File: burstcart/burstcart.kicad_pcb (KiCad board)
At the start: 2 copper layers, 56 x 91 mm, 17 parts, among them J1 IEC, J2 IEC, J3 BURST, J4 PORTA, U1 27C512, U2 CD74HCT4520E, U3 6526 CIA, U4 20V8, U5 ATtiny85-20P

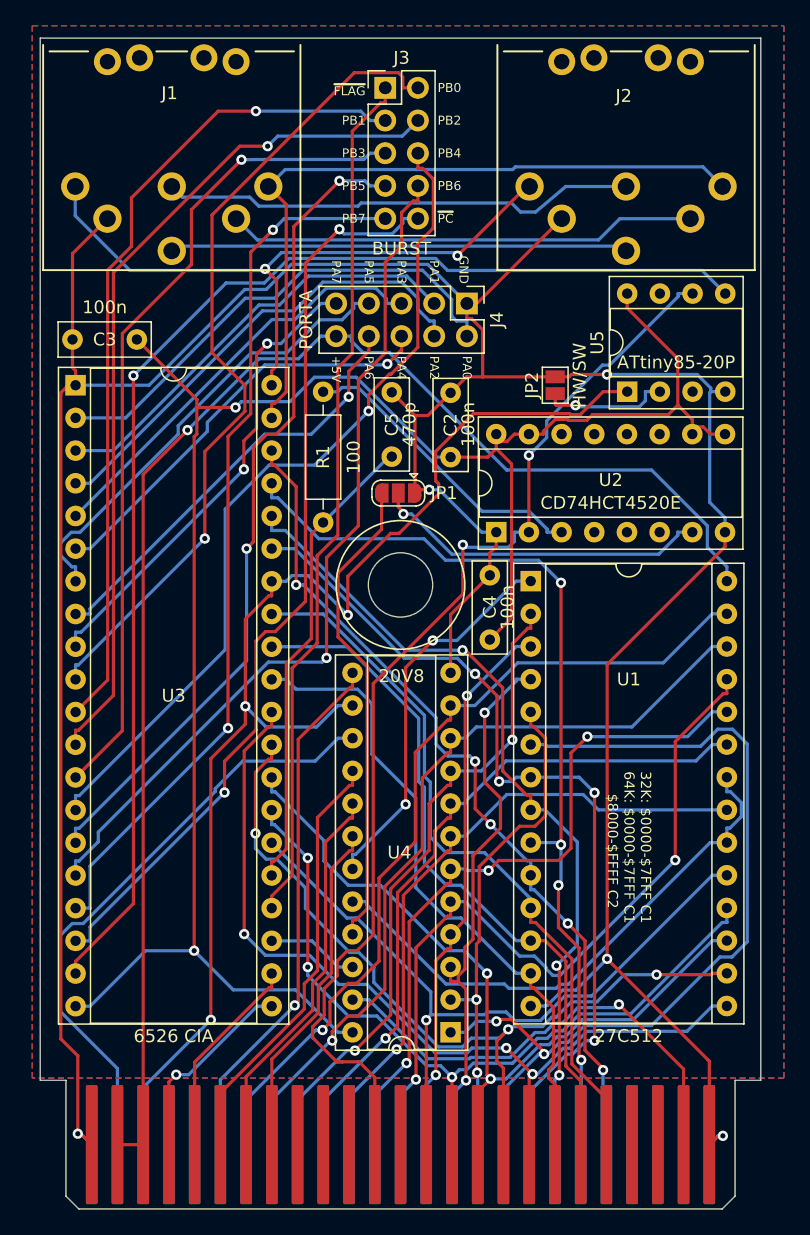
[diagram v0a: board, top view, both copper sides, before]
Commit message: - +5V net removed, all is VCC now - /CIA is pin 19, /ROM_A15 pin 22 now - default jumper shorted to reset CD4520 - default jumper shorted to phi2 for CIACLK - GAL is 22V10 - removed MUX connection to ATTINY - pullups for SP/CNT - silkscreen texts
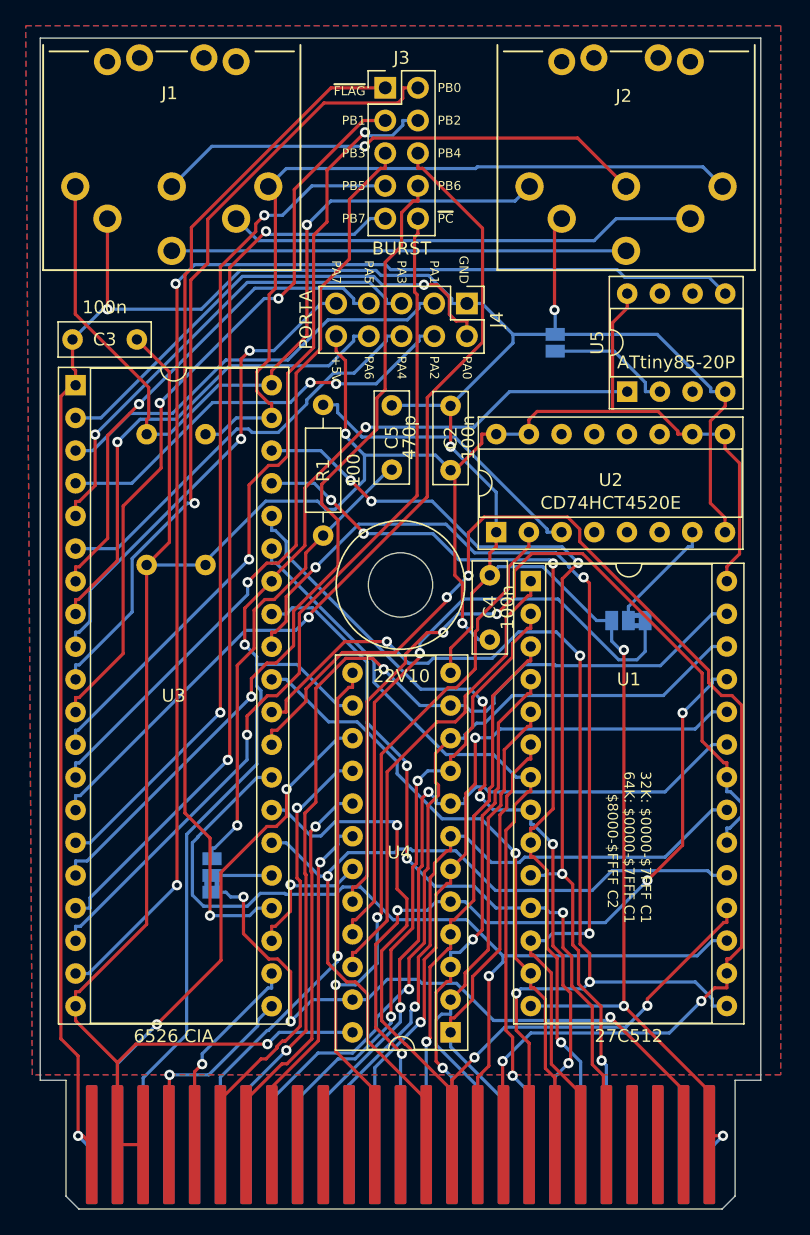
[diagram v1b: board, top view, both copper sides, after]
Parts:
- added JP3: O:HW/C:SW, Jumper:SolderJumper-2_P1.3mm_Open_Pad1.0x1.5mm, B.Cu at (160.3, 75.4)
- added R2: 3K3, Resistor_THT:R_Axial_DIN0207_L6.3mm_D2.5mm_P10.16mm_Horizontal, B.Cu at (133.1, 92.7)
- added R3: 3K3, Resistor_THT:R_Axial_DIN0207_L6.3mm_D2.5mm_P10.16mm_Horizontal, B.Cu at (128.5, 92.7)
- JP1: value Jumper_3_Open -> Jumper_3_Bridged12; footprint Jumper:SolderJumper-3_P1.3mm_Open_RoundedPad1.0x1.5mm -> Jumper:SolderJumper-3_P1.3mm_Bridged2Bar12_Pad1.0x1.5mm_NumberLabels; moved to B.Cu
- JP2: value HW/SW -> Jumper_3_Bridged12; footprint Jumper:SolderJumper-2_P1.3mm_Open_Pad1.0x1.5mm -> Jumper:SolderJumper-3_P1.3mm_Bridged2Bar12_Pad1.0x1.5mm_NumberLabels; moved to B.Cu
- U4: value 20V8 -> 22V10
- moved JP2 46.5 mm to (133.6, 116.8)
- moved JP1 20.4 mm to (166.0, 97.0)
- moved C5 1.02 mm to (147.6, 85.3)
- moved R1 1.02 mm to (142.2, 90.4)
- moved C2 1.02 mm to (152.1, 85.3)
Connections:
- C2 pad 1: +5V -> VCC
- C3 pad 1: +5V -> VCC
- C4 pad 1: +5V -> VCC
- C5 pad 1: /ciaclk -> Net-(C5-Pad1)
- J4 pad 10: /VCC -> VCC
- JP1 pad 1: GND -> /reset
- JP1 pad 3: /reset -> GND
- JP2 pad 1: Net-(JP2-Pad1) -> /PHI2
- JP2 pad 2: GND -> /ciaclk
- R1 pad 1: /ciaclk -> Net-(C5-Pad1)
- U$1 pad 2: /VCC -> VCC
- U$1 pad 3: /VCC -> VCC
- U1 pad 28: /VCC -> VCC
- U2 pad 10: +5V -> VCC
- U2 pad 15: +5V -> VCC
- U2 pad 16: +5V -> VCC
- U2 pad 9: +5V -> VCC
- U3 pad 20: +5V -> VCC
- U4 pad 19: /ROM_A15 -> /~{CIA}
- U4 pad 22: /~{CIA} -> /ROM_A15
- U4 pad 24: +5V -> VCC
- U5 pad 2: Net-(JP2-Pad1) -> Net-(JP3-Pad1)
- U5 pad 6: /MUX -> unconnected-(U5-Pad6)
- U5 pad 8: +5V -> VCC
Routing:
- net VCC: track 0.00 -> 190.3 mm, vias 0 -> 3
- net +5V: track 149.9 -> 0.00 mm, vias 2 -> 0
- net /VCC: track 113.6 -> 0.00 mm, vias 1 -> 0
- net /D4: track 65.3 -> 103.2 mm, vias 3 -> 4
- net Net-(C5-Pad1): track 0.00 -> 36.5 mm, vias 0 -> 1
- net /MUX: track 86.3 -> 52.2 mm
- net /A4: track 65.9 -> 32.2 mm, vias 2 -> 0
- net /ciaclk: track 36.5 -> 4.64 mm
- net /~{ROMCS}: track 43.0 -> 67.9 mm, vias 0 -> 2
- net /D1: track 54.1 -> 78.0 mm, vias 0 -> 3
- net Net-(U2-Pad7): track 26.4 -> 9.10 mm, vias 1 -> 0
- net /D3: track 68.4 -> 84.9 mm, vias 3 -> 4
- net IEC_SRQ: track 51.6 -> 65.1 mm, vias 2 -> 1
- net /PHI2: track 37.3 -> 49.9 mm, vias 1 -> 3
- net /D5: track 61.3 -> 73.1 mm, vias 2 -> 1
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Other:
- board text added: "3-2: SLOW 2-1: FAST"
- board text added: "BurstCart+4 v1.1 Maciej <ytm@elysium.pl> Witkowiak, V 2025"
- board text removed: "BurstCart+4 v1.0 Maciej <ytm@elysium.pl> Witkowiak, IV 2025"
